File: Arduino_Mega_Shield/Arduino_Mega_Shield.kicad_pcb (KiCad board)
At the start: 2 copper layers, 101.6 x 53.4 mm, 37 parts, among them J1 Conn_01x04, J10 Conn_01x02, J11 Conn_01x02, J12 Conn_01x02, J13 Conn_01x02, J14 Conn_01x02, J15 Motor Driver Connector, J16 Motor Driver Connector, J17 Motor Driver Connector, J18 Motor Driver Connector, J2 Conn_01x04, J3 Conn_01x04, J4 Conn_01x04, J5 Conn_01x02, J6 Conn_01x02, J7 Conn_01x02, J8 Conn_01x02, J9 Conn_01x02

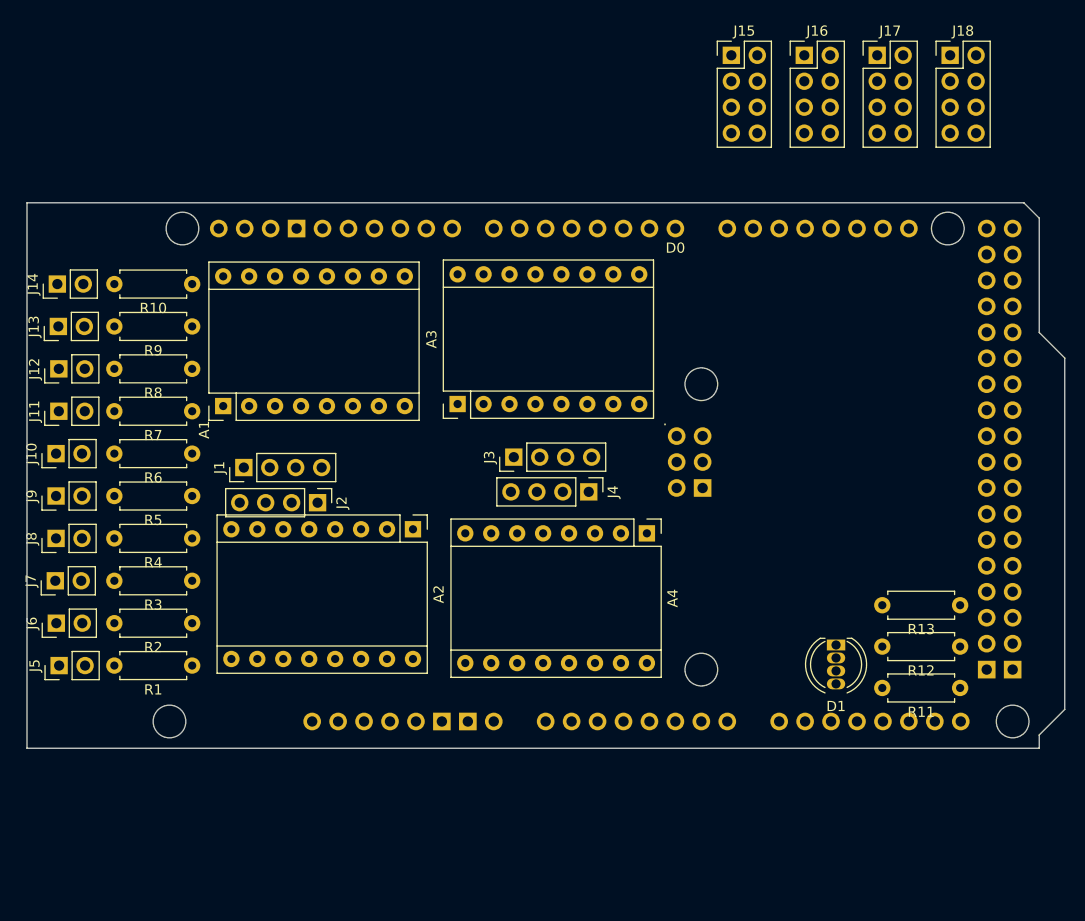
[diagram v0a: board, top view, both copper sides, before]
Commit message: Update KiCad PCB (Pololu A4988) and ESP32 code
Replace Arduino Mega shield footprint with a Pololu A4988 breakout footprint and reorganize PCB item positions/annotations (silkscreen, fab, footprint properties, net index adjustments). Add several Arduino_Mega_Shield backup zip files. Also include changes to ESP-32 embedded code (src/main.cpp and src/motor_constants.hpp) — likely motor/driver-related updates to match the hardware footprint changes.
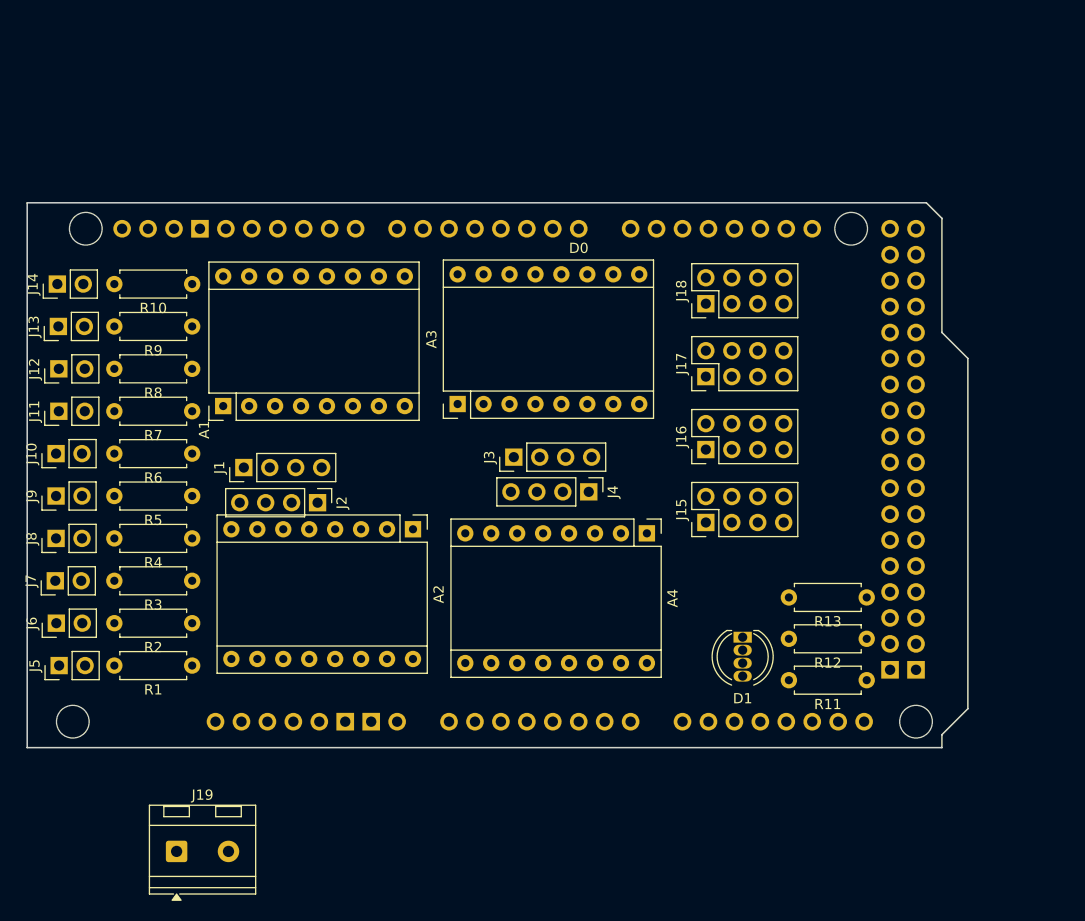
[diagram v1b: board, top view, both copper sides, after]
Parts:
- added J19: Screw_Terminal_01x02, TerminalBlock_RND:TerminalBlock_RND_205-00232_1x02_P5.08mm_Horizontal, F.Cu at (117.3, 127.0)
- moved J15 45.8 mm to (169.2, 94.8), turned to 90 degrees
- moved J16 39.8 mm to (169.2, 87.7), turned to 90 degrees
- moved J17 35.7 mm to (169.2, 80.5), turned to 90 degrees
- moved J18 34.1 mm to (169.2, 73.4), turned to 90 degrees
- moved A5 9.46 mm to (93.2, 116.8)
- moved D1 9.18 mm to (172.8, 106.0)
- moved R11 9.18 mm to (184.9, 110.2)
- moved R12 9.18 mm to (184.9, 106.2)
- moved R13 9.18 mm to (184.9, 102.1)
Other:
- board size 101.6 x 53.4 mm -> 92.1 x 53.3 mm

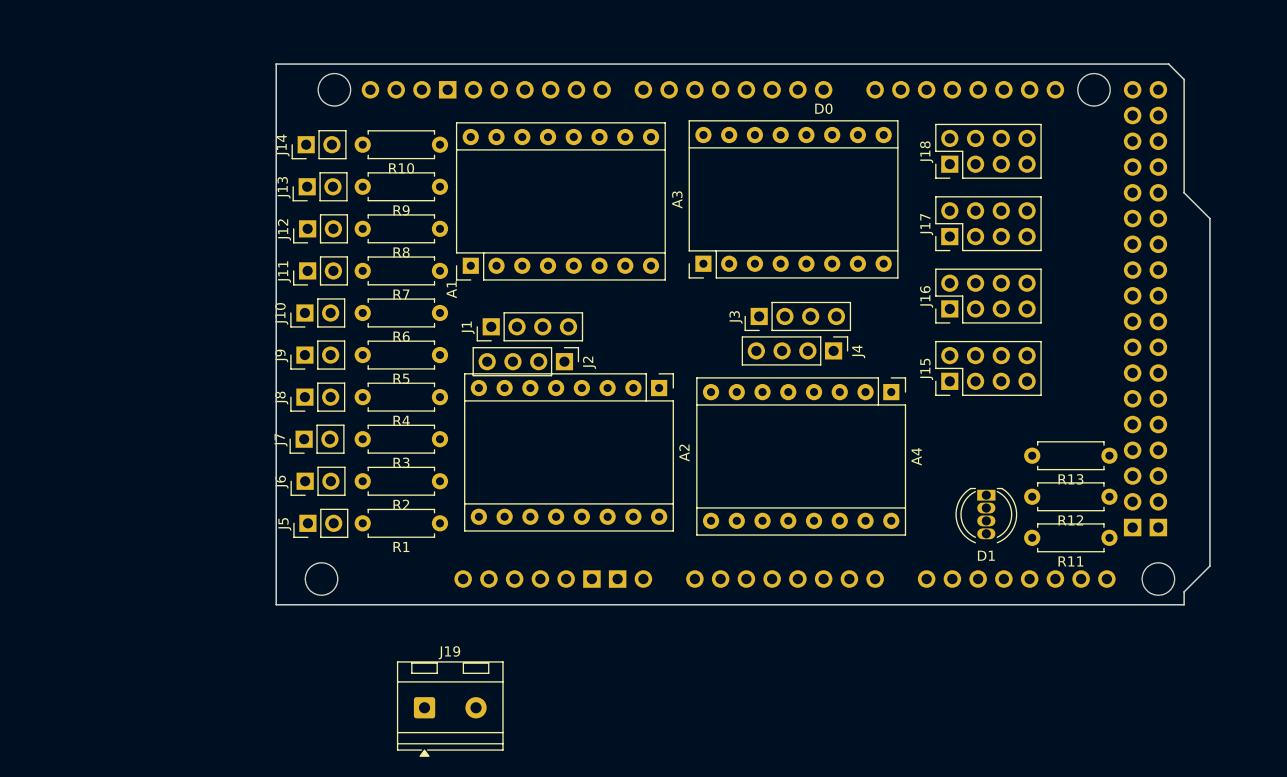
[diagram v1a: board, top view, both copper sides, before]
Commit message: Revise KiCad PCB footprints and add backups
Large update to the Arduino_Mega_Shield KiCad project: modified .kicad_pcb/.kicad_prl/.kicad_pro/.kicad_sch to replace and update connector footprints (JST XH, pin headers), adjust pad shapes/drills, 3D model refs, net names and UUIDs. Project housekeeping: removed autosave and lock files, renamed an autosave schematic to a .kicad_sch-bak, added multiple Arduino_Mega_Shield-backups ZIPs and added freerouting.rules. These changes consolidate footprint fixes and clean up temporary files prior to routing.
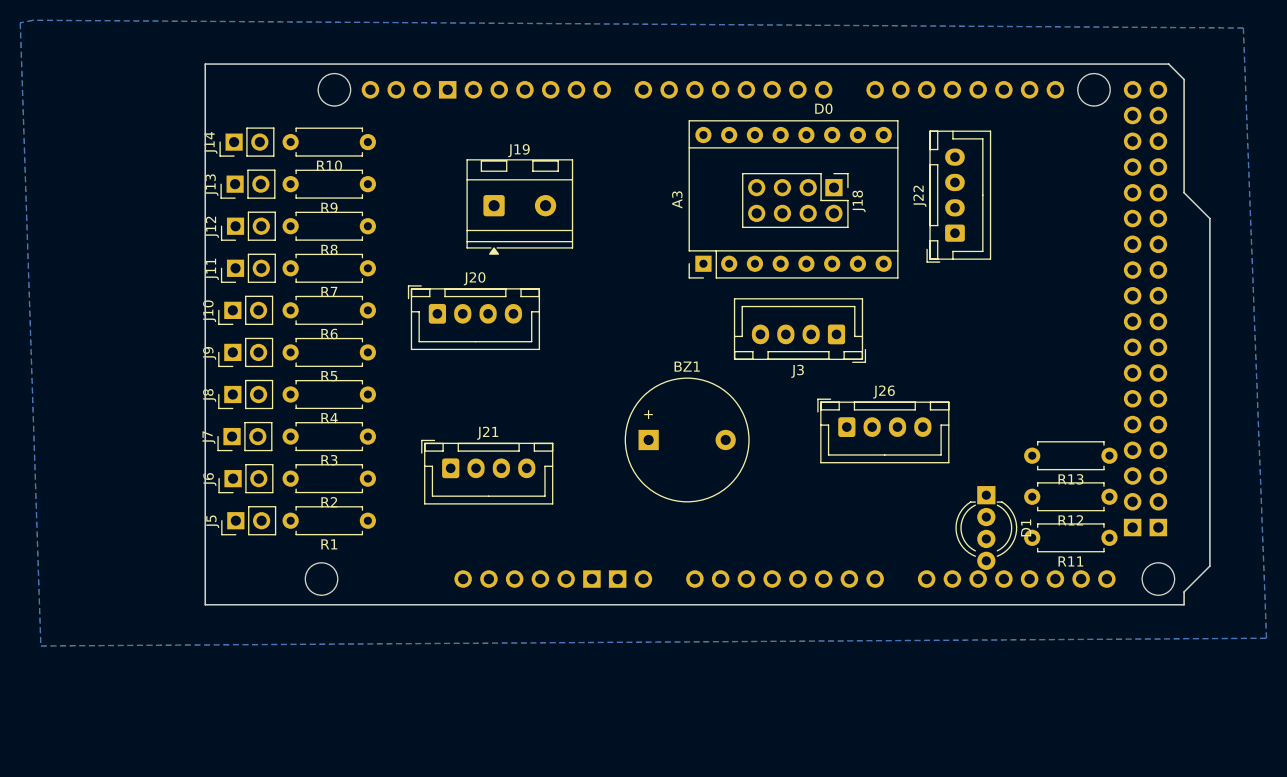
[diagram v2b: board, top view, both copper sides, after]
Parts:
- removed A1, A2, A4: Pololu_Breakout_A4988, Module:Pololu_Breakout-16_15.2x20.3mm
- removed J1, J2, J4: Conn_01x04, Connector_PinHeader_2.54mm:PinHeader_1x04_P2.54mm_Vertical
- removed J15, J16, J17: Motor Driver Connector, Connector_PinHeader_2.54mm:PinHeader_2x04_P2.54mm_Vertical
- added BZ1: Buzzer, Buzzer_Beeper:Buzzer_12x9.5RM7.6, F.Cu at (139.5, 100.6)
- added J20: JOYSTICK, Connector_JST:JST_XH_B4B-XH-A_1x04_P2.50mm_Vertical, F.Cu at (118.6, 88.1)
- added J21: I2C CONNECTOR, Connector_JST:JST_XH_B4B-XH-A_1x04_P2.50mm_Vertical, F.Cu at (119.9, 103.4)
- added J22: ENCODER1, Connector_JST:JST_XH_B4B-XH-A_1x04_P2.50mm_Vertical, F.Cu at (169.7, 80.2)
- added J26: I2C CONNECTOR, Connector_JST:JST_XH_B4B-XH-A_1x04_P2.50mm_Vertical, F.Cu at (159.0, 99.3)
- D1: value LED_RGBK -> LED_RKGB; footprint LED_THT:LED_D5.0mm-4_RGB -> LED_THT:LED_D5.0mm-4_RGB_Wide_Pins
- J10: value Conn_01x02 -> SW10
- J11: value Conn_01x02 -> SW6
- J12: value Conn_01x02 -> SW7
- J13: value Conn_01x02 -> SW8
- J14: value Conn_01x02 -> SW9
- J3: footprint Connector_PinHeader_2.54mm:PinHeader_1x04_P2.54mm_Vertical -> Connector_JST:JST_XH_B4B-XH-A_1x04_P2.50mm_Vertical
- J5: value Conn_01x02 -> SW5
- J6: value Conn_01x02 -> SW1
- J7: value Conn_01x02 -> SW2
- J8: value Conn_01x02 -> SW3
- J9: value Conn_01x02 -> SW4
- moved J19 50.0 mm to (124.2, 77.5)
- moved J18 11.7 mm to (157.7, 75.7), turned to -90 degrees
- moved J3 7.83 mm to (158.0, 90.2), turned to 180 degrees
- moved J10 7.12 mm to (98.4, 87.8)
- moved J11 7.12 mm to (98.7, 83.6)
- moved J12 7.12 mm to (98.7, 79.5)
- moved J13 7.12 mm to (98.7, 75.3)
- moved J14 7.12 mm to (98.6, 71.2)
- moved J5 7.12 mm to (98.7, 108.5)
- moved J6 7.12 mm to (98.5, 104.4)
- moved J7 7.12 mm to (98.4, 100.2)
- moved J8 7.12 mm to (98.4, 96.1)
- moved J9 7.12 mm to (98.4, 91.9)
- moved R1 7.12 mm to (111.8, 108.5)
- moved R10 7.12 mm to (111.8, 71.2)
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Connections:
- A5 pad 5V1: unconnected-(A5-5V-Pad5V1) -> +5V
- A5 pad 5V3: unconnected-(A5-5V-Pad5V3) -> +5V
- A5 pad 5V4: unconnected-(A5-5V-Pad5V4) -> +5V
- A5 pad A0: unconnected-(A5-PadA0) -> VRX
- A5 pad A1: unconnected-(A5-PadA1) -> VRY
- A5 pad A2: unconnected-(A5-PadA2) -> LEDR
- A5 pad A3: unconnected-(A5-PadA3) -> LEDG
- A5 pad A4: unconnected-(A5-PadA4) -> LEDB
- A5 pad A5: unconnected-(A5-PadA5) -> BUZZER
- A5 pad D10: unconnected-(A5-PadD10) -> RPWM3
- A5 pad D11: unconnected-(A5-PadD11) -> LPWM3
- A5 pad D12: unconnected-(A5-PadD12) -> RPWM4
- A5 pad D13: unconnected-(A5-PadD13) -> LPWM4
- A5 pad D16: unconnected-(A5-D16/TX2-PadD16) -> TX2
- A5 pad D17: unconnected-(A5-D17/RX2-PadD17) -> RX2
- A5 pad D18: unconnected-(A5-D18/TX1-PadD18) -> ENC_A3
- A5 pad D19: unconnected-(A5-D19/RX1-PadD19) -> ENC_A4
- A5 pad D20: unconnected-(A5-D20/SDA-PadD20) -> SDA
- A5 pad D21: unconnected-(A5-D21/SCL-PadD21) -> SCL
- A5 pad D22: unconnected-(A5-PadD22) -> R_EN1
- A5 pad D23: unconnected-(A5-PadD23) -> L_EN1
- A5 pad D24: unconnected-(A5-PadD24) -> R_EN2
- A5 pad D25: unconnected-(A5-PadD25) -> L_EN2
- A5 pad D26: unconnected-(A5-PadD26) -> R_EN3
- A5 pad D27: unconnected-(A5-PadD27) -> L_EN3
- A5 pad D28: unconnected-(A5-PadD28) -> R_EN4
- A5 pad D29: unconnected-(A5-PadD29) -> L_EN4
- A5 pad D30: unconnected-(A5-PadD30) -> R_IS1
- A5 pad D31: unconnected-(A5-PadD31) -> L_IS1
- A5 pad D32: unconnected-(A5-PadD32) -> R_IS2
- A5 pad D33: unconnected-(A5-PadD33) -> L_IS2
- A5 pad D34: unconnected-(A5-PadD34) -> R_IS3
- A5 pad D35: unconnected-(A5-PadD35) -> L_IS3
- A5 pad D36: unconnected-(A5-PadD36) -> R_IS4
- A5 pad D37: unconnected-(A5-PadD37) -> L_IS4
- A5 pad D38: unconnected-(A5-PadD38) -> SW1
- A5 pad D39: unconnected-(A5-PadD39) -> SW2
- A5 pad D40: unconnected-(A5-PadD40) -> SW3
- A5 pad D41: unconnected-(A5-PadD41) -> SW4
- A5 pad D42: unconnected-(A5-PadD42) -> SW5
- A5 pad D43: unconnected-(A5-PadD43) -> SW6
- A5 pad D44: unconnected-(A5-PadD44) -> SW7
- A5 pad D45: unconnected-(A5-PadD45) -> SW8
- A5 pad D46: unconnected-(A5-PadD46) -> SW9
- A5 pad D47: unconnected-(A5-PadD47) -> SW10
- A5 pad D48: unconnected-(A5-PadD48) -> ENC_B1
- A5 pad D49: unconnected-(A5-PadD49) -> ENC_B2
- A5 pad D50: unconnected-(A5-D50_MISO-PadD50) -> ENC_B3
- A5 pad D51: unconnected-(A5-D51_MOSI-PadD51) -> ENC_B4
- A5 pad D6: unconnected-(A5-PadD6) -> RPWM1
- A5 pad D7: unconnected-(A5-PadD7) -> LPWM1
- A5 pad D8: unconnected-(A5-PadD8) -> RPWM2
- A5 pad D9: unconnected-(A5-PadD9) -> LPWM2
- A5 pad GND1: unconnected-(A5-GND-PadGND1) -> GND
- A5 pad GND2: unconnected-(A5-GND-PadGND2) -> GND
- A5 pad GND3: unconnected-(A5-GND-PadGND3) -> GND
- A5 pad GND5: unconnected-(A5-GND-PadGND5) -> GND
- A5 pad GND6: unconnected-(A5-GND-PadGND6) -> GND
- A5 pad SCL: unconnected-(A5-PadSCL) -> SCL
- A5 pad SDA: unconnected-(A5-PadSDA) -> SDA
- A5 pad VIN: unconnected-(A5-PadVIN) -> +12V
- D1 pad 2: Net-(D1-GA) -> GND
- D1 pad 3: Net-(D1-BA) -> Net-(D1-GA)
- D1 pad 4: GND -> Net-(D1-BA)
- J10 pad 2: Net-(J10-Pin_2) -> SW10
- J11 pad 2: Net-(J11-Pin_2) -> SW6
- J12 pad 2: Net-(J12-Pin_2) -> SW7
- J13 pad 2: Net-(J13-Pin_2) -> SW8
- J14 pad 2: Net-(J14-Pin_2) -> SW9
- J18 pad 1: unconnected-(J18-Pin_1-Pad1) -> RPWM4
- J18 pad 2: unconnected-(J18-Pin_2-Pad2) -> LPWM4
- J18 pad 3: unconnected-(J18-Pin_3-Pad3) -> R_EN4
- J18 pad 4: unconnected-(J18-Pin_4-Pad4) -> L_EN4
- J18 pad 5: unconnected-(J18-Pin_5-Pad5) -> R_IS4
- J18 pad 6: unconnected-(J18-Pin_6-Pad6) -> L_IS4
- J18 pad 7: unconnected-(J18-Pin_7-Pad7) -> +5V
- J18 pad 8: unconnected-(J18-Pin_8-Pad8) -> GND
- J19 pad 1: unconnected-(J19-Pin_1-Pad1) -> +12V
- J19 pad 2: unconnected-(J19-Pin_2-Pad2) -> GND
- J5 pad 2: Net-(J5-Pin_2) -> SW5
- J6 pad 2: Net-(J6-Pin_2) -> SW1
- J7 pad 2: Net-(J7-Pin_2) -> SW2
- J8 pad 2: Net-(J8-Pin_2) -> SW3
- J9 pad 2: Net-(J9-Pin_2) -> SW4
- R1 pad 2: Net-(J5-Pin_2) -> SW5
- R10 pad 2: Net-(J14-Pin_2) -> SW9
- R11 pad 1: unconnected-(R11-Pad1) -> LEDB
- R12 pad 1: unconnected-(R12-Pad1) -> LEDG
- R13 pad 1: unconnected-(R13-Pad1) -> LEDR
- R2 pad 2: Net-(J6-Pin_2) -> SW1
- R3 pad 2: Net-(J7-Pin_2) -> SW2
- R4 pad 2: Net-(J8-Pin_2) -> SW3
- R5 pad 2: Net-(J9-Pin_2) -> SW4
- R6 pad 2: Net-(J10-Pin_2) -> SW10
- R7 pad 2: Net-(J11-Pin_2) -> SW6
- R8 pad 2: Net-(J12-Pin_2) -> SW7
- R9 pad 2: Net-(J13-Pin_2) -> SW8
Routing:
- added copper zone on B.Cu, net GND
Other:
- board size 92.1 x 53.3 mm -> 99.1 x 53.3 mm

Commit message: Avancement on the electric shemas and some fixe on the PCB
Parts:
- moved J21 57.9 mm to (123.8, 161.2)
- moved J20 57.9 mm to (122.5, 145.9)
- moved BZ1 52.3 mm to (103.6, 138.7)
- moved J14 46.2 mm to (116.5, 113.8), turned to 180 degrees
- moved J26 41.4 mm to (152.0, 140.1)
- moved R10 29.8 mm to (116.5, 100.6), turned to -90 degrees
- moved J19 27.5 mm to (99.1, 66.3), turned to -90 degrees
- moved J3 8.06 mm to (149.9, 89.7), turned to 0 degrees
- moved D1 2.91 mm to (172.6, 103.1)
- moved J13 1.20 mm to (98.4, 76.5)
- moved R9 1.20 mm to (111.5, 76.5)
- moved J12 1.09 mm to (98.5, 80.6)
- moved R8 1.09 mm to (111.5, 80.6)
- moved J11 0.97 mm to (98.5, 84.6)
- moved R7 0.97 mm to (111.5, 84.6)
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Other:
- board size 99.1 x 53.3 mm -> 99.5 x 53.3 mm
